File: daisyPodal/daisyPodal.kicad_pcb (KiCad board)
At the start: 2 copper layers, 76 x 80 mm, 39 parts, among them J1 Guitar in, J2 Left out, J3 fsw pin 1, J4 fsw pin 4, J5 fsw pin 6, J6 fsw pin 3, J7 fsw pin 2, J8 fsw pin 5, SW1 Switch 1, SW2 Switch 2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

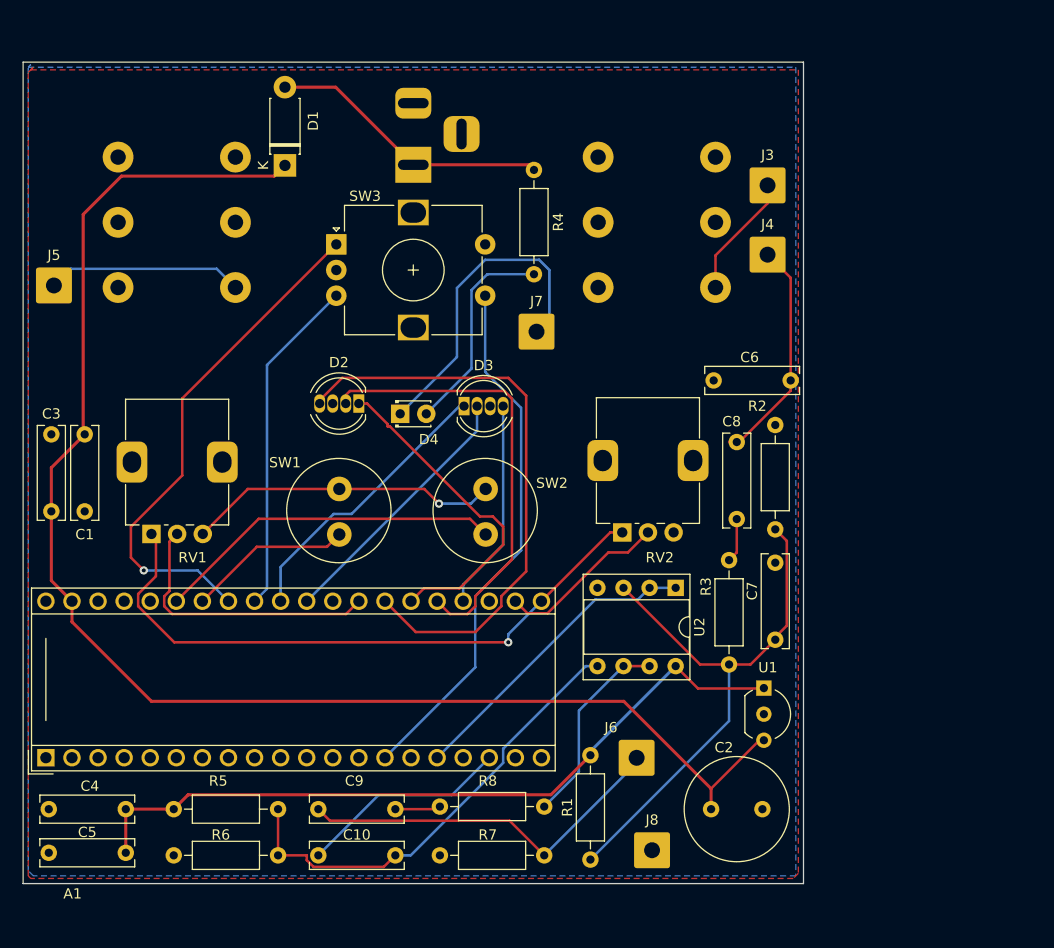
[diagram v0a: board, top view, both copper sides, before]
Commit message: Sort out correct RGB LEDS - RAGB
Common anode on the Pod
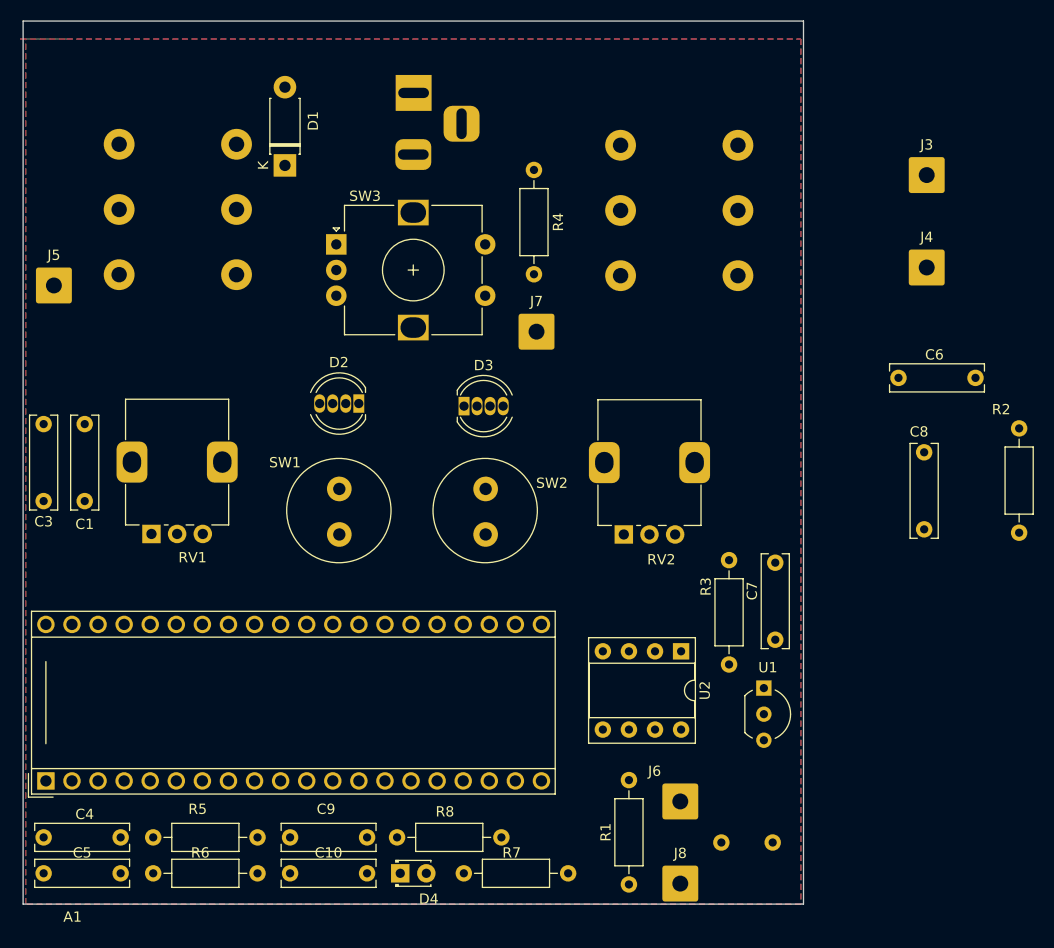
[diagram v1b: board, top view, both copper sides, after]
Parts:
- BT1: footprint Connector_BarrelJack:BarrelJack_Horizontal -> Connector_BarrelJack:BarrelJack_Horizontal_centre_negative
- C2: moved to B.Cu
- moved D4 44.8 mm to (136.7, 119.0)
- moved R2 23.8 mm to (197.0, 85.8)
- moved C8 18.3 mm to (187.8, 78.0)
- moved C6 18.0 mm to (192.8, 70.8)
- moved J4 15.6 mm to (188.0, 60.0)
- moved J3 15.5 mm to (188.0, 51.0)
- moved C2 6.82 mm to (173.0, 116.0), turned to 180 degrees
- moved C3 6.54 mm to (102.0, 82.8), turned to 90 degrees
- moved U2 6.20 mm to (164.1, 97.4)
- moved J6 6.01 mm to (164.0, 112.0)
- moved R8 5.14 mm to (146.6, 115.5)
- moved R1 4.46 mm to (159.0, 109.9)
- moved J8 4.26 mm to (164.0, 120.0)
- moved C9 3.89 mm to (133.5, 115.5)
- moved R5 3.40 mm to (112.7, 115.5)
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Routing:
- net /VCC: track 141.6 -> 0.00 mm
- net +5V: track 73.5 -> 0.00 mm
- net /3v3: track 61.4 -> 0.00 mm, vias 1 -> 0
- net /LED_1_R: track 56.7 -> 0.00 mm
- net Net-(U2A-+): track 55.7 -> 0.00 mm
- net /ENC_CLICK: track 51.9 -> 0.00 mm
- net Net-(A1-SAI2_SD_A): track 50.0 -> 0.00 mm, vias 1 -> 0
- net Net-(U2B-+): track 45.2 -> 0.00 mm
- net /LED_1_B: track 43.7 -> 0.00 mm
- net Net-(J6-Pin_1): track 37.1 -> 0.00 mm
- net Net-(A1-SAI2_SCK): track 34.1 -> 0.00 mm
- net Net-(A1-SAI2_SD_B): track 33.0 -> 0.00 mm
- net GND: track 32.5 -> 0.00 mm, vias 1 -> 0
- net /LED_1_G: track 32.2 -> 0.00 mm
- net Net-(D4-K): track 31.6 -> 0.00 mm
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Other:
- board size 76 x 80 mm -> 76 x 86 mm

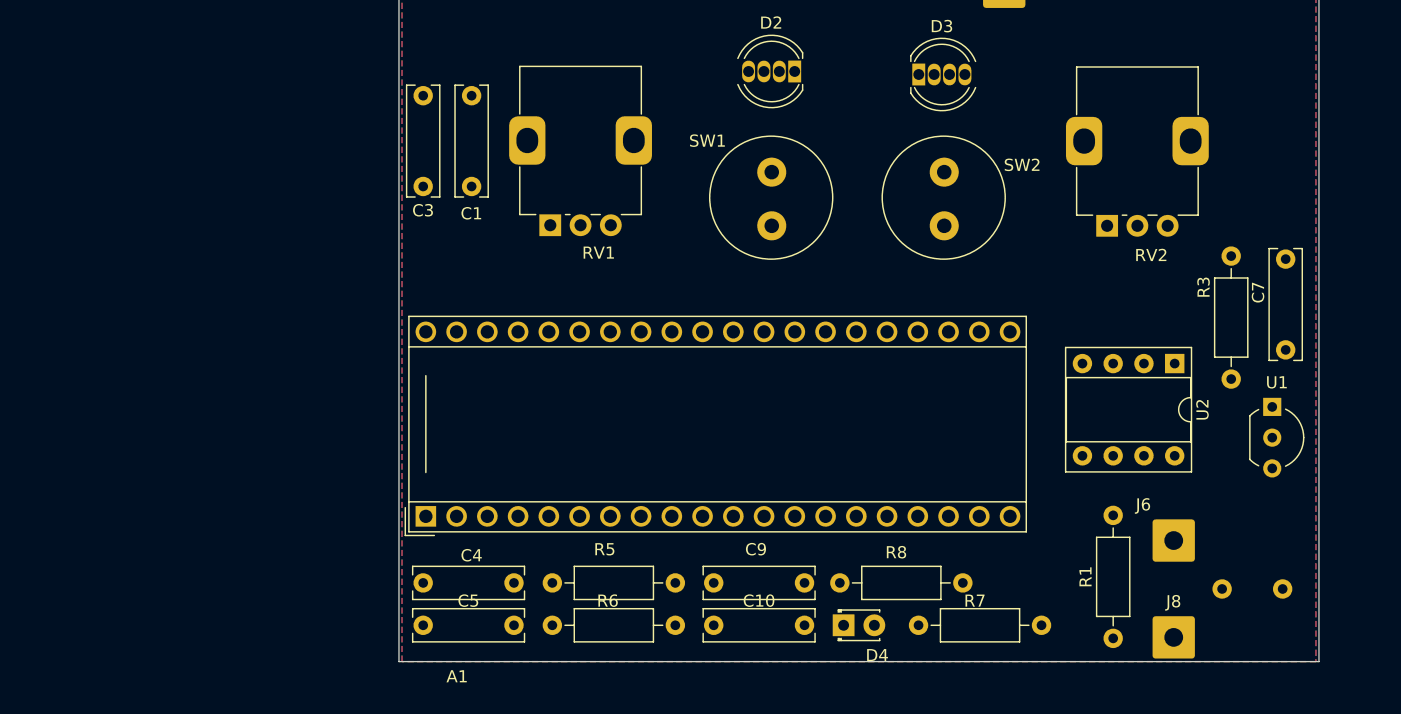
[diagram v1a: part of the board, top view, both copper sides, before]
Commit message: Increase hole size of pads for LM7805
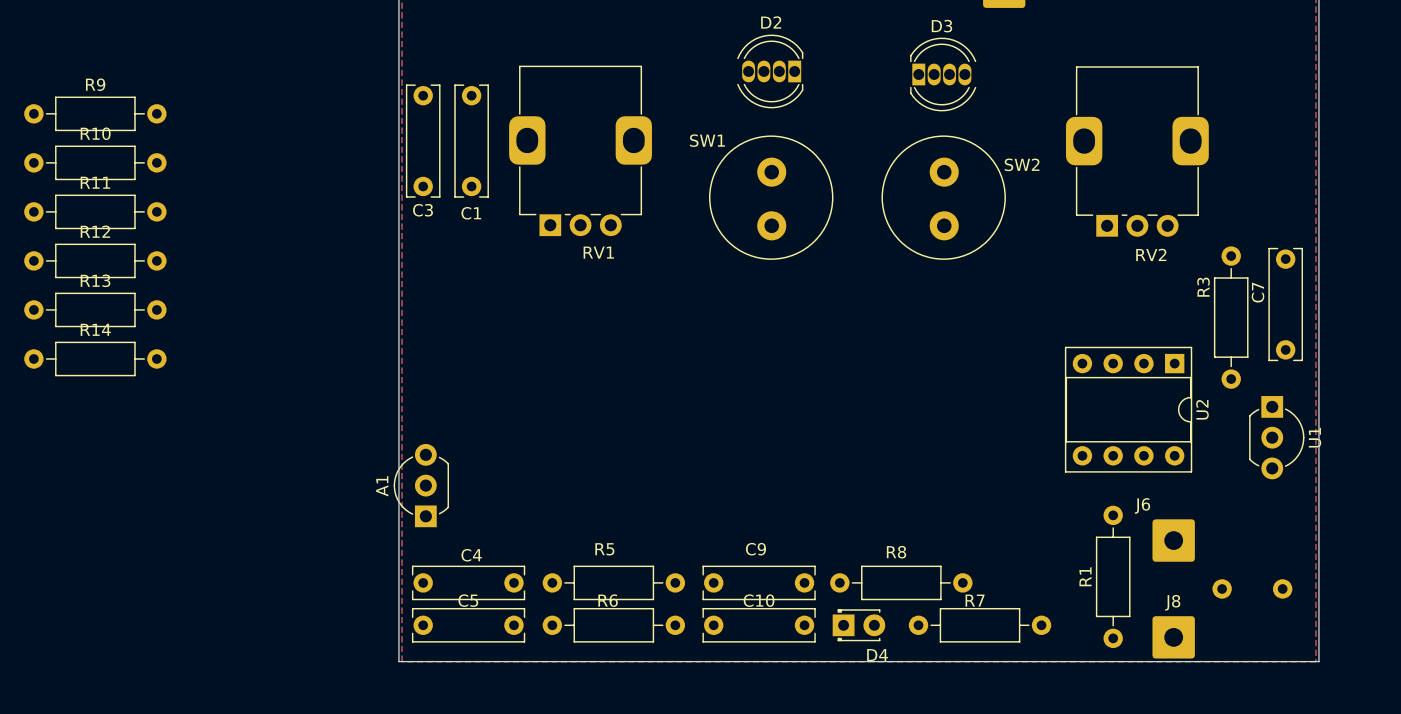
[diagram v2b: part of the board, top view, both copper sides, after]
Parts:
- added R10: 1k, Resistor_THT:R_Axial_DIN0207_L6.3mm_D2.5mm_P10.16mm_Horizontal, F.Cu at (69.8, 80.8)
- added R11: 1k, Resistor_THT:R_Axial_DIN0207_L6.3mm_D2.5mm_P10.16mm_Horizontal, F.Cu at (69.8, 84.8)
- added R12: 1k, Resistor_THT:R_Axial_DIN0207_L6.3mm_D2.5mm_P10.16mm_Horizontal, F.Cu at (69.8, 88.9)
- added R13: 1k, Resistor_THT:R_Axial_DIN0207_L6.3mm_D2.5mm_P10.16mm_Horizontal, F.Cu at (69.8, 93.0)
- added R14: 1k, Resistor_THT:R_Axial_DIN0207_L6.3mm_D2.5mm_P10.16mm_Horizontal, F.Cu at (69.8, 97.0)
- added R9: 1k, Resistor_THT:R_Axial_DIN0207_L6.3mm_D2.5mm_P10.16mm_Horizontal, F.Cu at (69.8, 76.8)
- A1: footprint Module:Electrosmith_Daisy_Seed -> Package_TO_SOT_THT:TO-92_Inline_Wide_78L05_dc
- U1: footprint Package_TO_SOT_THT:TO-92_Inline_Wide -> Package_TO_SOT_THT:TO-92_Inline_Wide_78L05_dc
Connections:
- RV1 pad 1: /3v3 -> GND
- RV1 pad 3: GND -> /3v3
- RV2 pad 1: /3v3 -> GND
- RV2 pad 3: GND -> /3v3

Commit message: Flip LM7805 to back of board
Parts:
- U1: moved to B.Cu
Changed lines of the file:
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@@
-    )
-  )
-  (footprint "Package_TO_SOT_THT:TO-92_Inline_Wide_78L05_dc" (layer "F.Cu")
-    (at 172.14 100.96 -90)
-    (descr "TO-92 leads in-line, wide, drill 0.75mm (see NXP sot054_po.pdf)")
-    (tags "to-92 sc-43 sc-43a sot54 PA33 transistor")
-    (property "Sheetfile" "daisyPodal.kicad_sch")
-    (property "Sheetname" "")
-    (property "ki_description" "Positive 100mA 30V Linear Regulator, Fixed Output 5V, TO-92")
-    (property "ki_keywords" "Voltage Regulator 100mA Positive")
-    (attr through_hole)
-    (fp_text reference "U1" (at 2.54 -3.56 -90) (layer "F.SilkS")
-        (effects (font (size 1 1) (thickness 0.15)))
-    )
-    (fp_text value "L78L05_TO92" (at 2.54 2.79 -90) (layer "F.Fab")
-        (effects (font (size 1 1) (thickness 0.15)))
-    )
-    (fp_text user "${REFERENCE}" (at 2.54 0 -90) (layer "F.Fab")
-        (effects (font (size 1 1) (thickness 0.15)))
-    )
-    (fp_line (start 0.74 1.85) (end 4.34 1.85)
-      (stroke (width 0.12) (type solid)) (layer "F.SilkS"))
-    (fp_arc (start 0.1836 -1.098807) (mid 1.143021 -2.192817) (end 2.54 -2.6)
-      (stroke (width 0.12) (type solid)) (layer "F.SilkS"))
-    (fp_arc (start 0.74 1.85) (mid 0.446097 1.509328) (end 0.215816 1.122795)
-      (stroke (width 0.12) (type solid)) (layer "F.SilkS"))
-    (fp_arc (start 2.54 -2.6) (mid 3.936979 -2.192818) (end 4.8964 -1.098807)
-      (stroke (width 0.12) (type solid)) (layer "F.SilkS"))
-    (fp_arc (start 4.864184 1.122795) (mid 4.633903 1.509328) (end 4.34 1.85)
-      (stroke (width 0.12) (type solid)) (layer "F.SilkS"))
-    (fp_line (start -1.01 -2.73) (end -1.01 2.01)
-      (stroke (width 0.05) (type solid)) (layer "F.CrtYd"))
-    (fp_line (start -1.01 -2.73) (end 6.09 -2.73)
-      (stroke (width 0.05) (type solid)) (layer "F.CrtYd"))
-    (fp_line (start 6.09 2.01) (end -1.01 2.01)
-      (stroke (width 0.05) (type solid)) (layer "F.CrtYd"))
-    (fp_line (start 6.09 2.01) (end 6.09 -2.73)
-      (stroke (width 0.05) (type solid)) (layer "F.CrtYd"))
-    (fp_line (start 0.8 1.75) (end 4.3 1.75)
-      (stroke (width 0.1) (type solid)) (layer "F.Fab"))
-    (fp_arc (start 0.786375 1.753625) (mid 0.248779 -0.949055) (end 2.54 -2.48)
-      (stroke (width 0.1) (type solid)) (layer "F.Fab"))
-    (fp_arc (start 2.54 -2.48) (mid 4.831221 -0.949055) (end 4.293625 1.753625)
-      (stroke (width 0.1) (type solid)) (layer "F.Fab"))
-    (pad "1" thru_hole rect (at 0 0 270) (size 1.8 1.8) (drill 1) (layers "*.Cu" "*.Mask")
-      (net 23 "+5V") (pinfunction "VO") (pintype "power_out"))
-    (pad "2" thru_hole circle (at 2.54 0 270) (size 1.8 1.8) (drill 1) (layers "*.Cu" "*.Mask")
-      (net 7 "GND") (pinfunction "GND") (pintype "power_in"))
-    (pad "3" thru_hole circle (at 5.08 0 270) (size 1.8 1.8) (drill 1) (layers "*.Cu" "*.Mask")
-      (net 21 "/VCC") (pinfunction "VI") (pintype "power_in"))
-    (model "${KICAD6_3DMODEL_DIR}/Package_TO_SOT_THT.3dshapes/TO-92_Inline_Wide.wrl"
-      (offset (xyz 0 0 0))
-      (scale (xyz 1 1 1))
-      (rotate (xyz 0 0 0))
     )
   )
@@
       (offset (xyz 0 0 0))
       (scale (xyz 1 1 1))
+      (rotate (xyz 0 0 0))
+    )
+  )
+  (footprint "Package_TO_SOT_THT:TO-92_Inline_Wide_78L05_dc" (layer "B.Cu")
+    (at 172.14 100.96 -90)
+    (descr "TO-92 leads in-line, wide, drill 0.75mm (see NXP sot054_po.pdf)")
+    (tags "to-92 sc-43 sc-43a sot54 PA33 transistor")
+    (property "Sheetfile" "daisyPodal.kicad_sch")
+    (property "Sheetname" "")
+    (property "ki_description" "Positive 100mA 30V Linear Regulator, Fixed Output 5V, TO-92")
+    (property "ki_keywords" "Voltage Regulator 100mA Positive")
+    (attr through_hole)
+    (fp_text reference "U1" (at 2.54 3.56 90) (layer "B.SilkS")
+        (effects (font (size 1 1) (thickness 0.15)) (justify mirror))
+    )
+    (fp_text value "L78L05_TO92" (at 2.54 -2.79 90) (layer "B.Fab")
+        (effects (font (size 1 1) (thickness 0.15)) (justify mirror))
+    )
+    (fp_text user "${REFERENCE}" (at 2.54 0 90) (layer "B.Fab")
+        (effects (font (size 1 1) (thickness 0.15)) (justify mirror))
+    )
+    (fp_line (start 0.74 -1.85) (end 4.34 -1.85)
+      (stroke (width 0.12) (type solid)) (layer "B.SilkS"))
+    (fp_arc (start 0.215816 -1.122795) (mid 0.446097 -1.509328) (end 0.74 -1.85)
+      (stroke (width 0.12) (type solid)) (layer "B.SilkS"))
+    (fp_arc (start 2.54 2.6) (mid 1.143021 2.192818) (end 0.1836 1.098807)
+      (stroke (width 0.12) (type solid)) (layer "B.SilkS"))
+    (fp_arc (start 4.34 -1.85) (mid 4.633903 -1.509328) (end 4.864184 -1.122795)
+      (stroke (width 0.12) (type solid)) (layer "B.SilkS"))
+    (fp_arc (start 4.8964 1.098807) (mid 3.936979 2.192817) (end 2.54 2.6)
+      (stroke (width 0.12) (type solid)) (layer "B.SilkS"))
+    (fp_line (start -1.01 2.73) (end -1.01 -2.01)
+      (stroke (width 0.05) (type solid)) (layer "B.CrtYd"))
+    (fp_line (start -1.01 2.73) (end 6.09 2.73)
+      (stroke (width 0.05) (type solid)) (layer "B.CrtYd"))
+    (fp_line (start 6.09 -2.01) (end -1.01 -2.01)
+      (stroke (width 0.05) (type solid)) (layer "B.CrtYd"))
+    (fp_line (start 6.09 -2.01) (end 6.09 2.73)
+      (stroke (width 0.05) (type solid)) (layer "B.CrtYd"))
+    (fp_line (start 0.8 -1.75) (end 4.3 -1.75)
+      (stroke (width 0.1) (type solid)) (layer "B.Fab"))
+    (fp_arc (start 2.54 2.48) (mid 0.248779 0.949055) (end 0.786375 -1.753625)
+      (stroke (width 0.1) (type solid)) (layer "B.Fab"))
+    (fp_arc (start 4.293625 -1.753625) (mid 4.831221 0.949055) (end 2.54 2.48)
+      (stroke (width 0.1) (type solid)) (layer "B.Fab"))
+    (pad "1" thru_hole rect (at 0 0 270) (size 1.8 1.8) (drill 1) (layers "*.Cu" "*.Mask")
+      (net 23 "+5V") (pinfunction "VO") (pintype "power_out"))
+    (pad "2" thru_hole circle (at 2.54 0 270) (size 1.8 1.8) (drill 1) (layers "*.Cu" "*.Mask")
+      (net 7 "GND") (pinfunction "GND") (pintype "power_in"))
+    (pad "3" thru_hole circle (at 5.08 0 270) (size 1.8 1.8) (drill 1) (layers "*.Cu" "*.Mask")
+      (net 21 "/VCC") (pinfunction "VI") (pintype "power_in"))
+    (model "${KICAD6_3DMODEL_DIR}/Package_TO_SOT_THT.3dshapes/TO-92_Inline_Wide.wrl"
+      (offset (xyz 0 0 0))
+      (scale (xyz 1 1 1))
